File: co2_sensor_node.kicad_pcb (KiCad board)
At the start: 4 copper layers, 60 x 110 mm, 71 parts, among them J1 Conn_01x07_Female, J10 Conn_01x02_Male, J11 Conn_01x02_Male, J12 Conn_01x02_Male, J13 Conn_01x02_Male, J14 Conn_01x02, J15 Conn_01x06_Male, J2 Conn_01x04_Female, J3 Conn_01x07_Female, J4 Conn_01x04_Female, J5 Conn_01x04_Female, J6 TF-15x15, J7 SMA Female, J8 Conn_01x02_Male, J9 Conn_01x02_Male, Q1 AO3400A, Q2 AO3401A, Q3 AO3400A, Q4 AO3401A, Q5 AO3401A, SW1 K2-1102SP-C4SC-04, U1 RFM95W-868S2, U2 ublox_SAM-M8Q, U3 TPS62130, U4 TPS62130, U5 ESP32-WROOM-32D

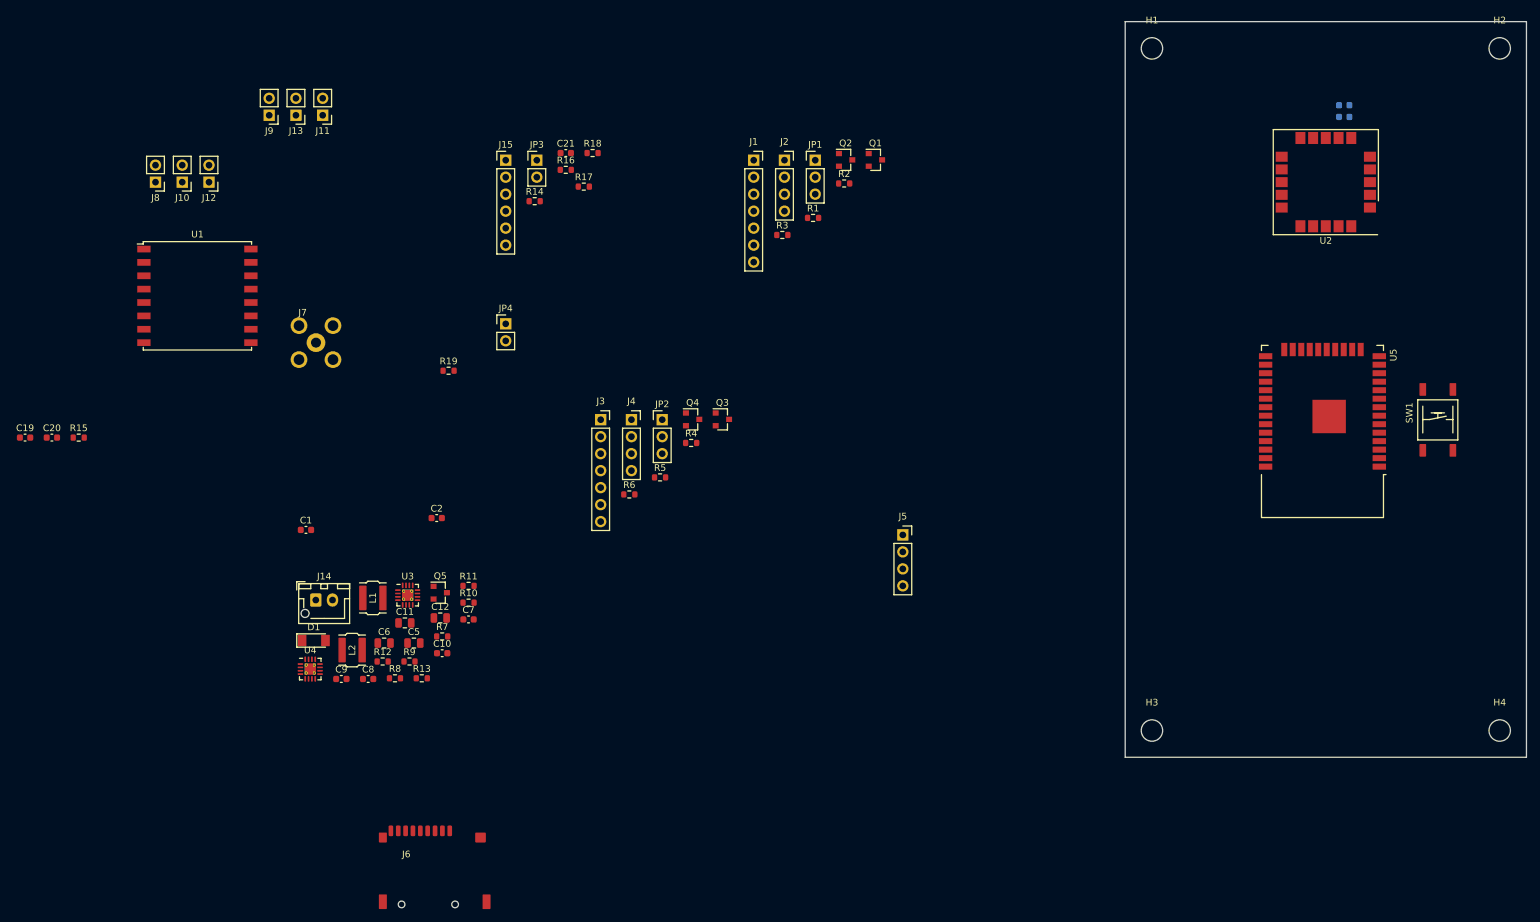
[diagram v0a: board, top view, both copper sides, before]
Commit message: First cut at layout
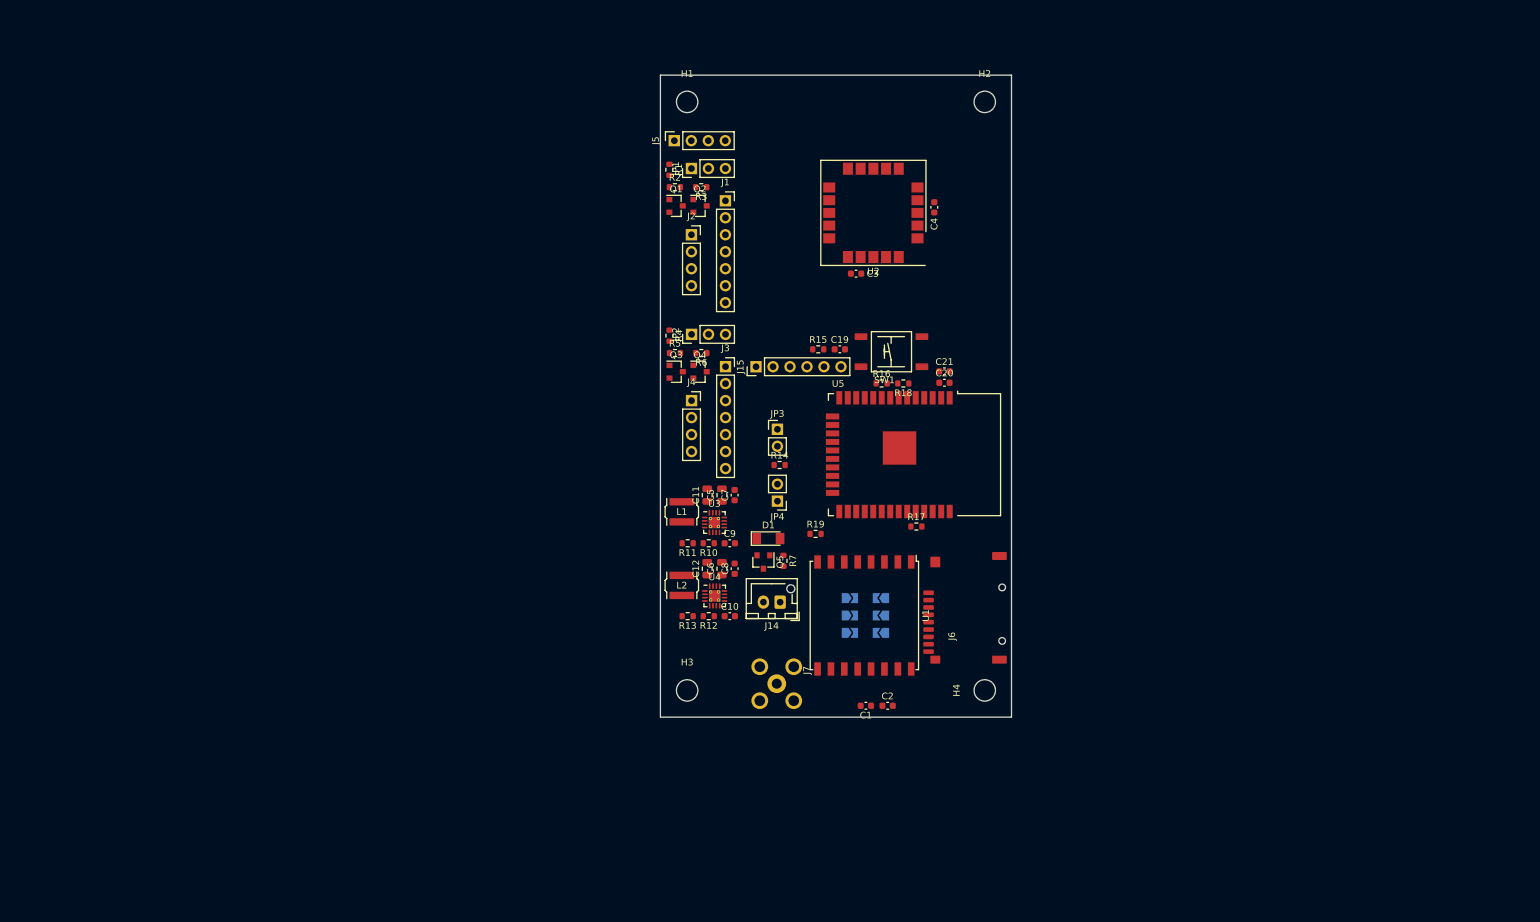
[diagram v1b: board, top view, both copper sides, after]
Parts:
- removed R8, R9: 100k, Resistor_SMD:R_0603_1608Metric
- C3, C4: moved to F.Cu
- J10, J11, J12, J13, J8, J9: footprint Connector_PinHeader_2.54mm:PinHeader_1x02_P2.54mm_Vertical -> Jumper:SolderJumper-2_P1.3mm_Open_TrianglePad1.0x1.5mm; moved to B.Cu
- moved C20 133.7 mm to (163.0, 90.0)
- moved J8 127.7 mm to (153.5, 127.4)
- moved J10 122.9 mm to (153.5, 124.8)
- moved C19 122.5 mm to (147.3, 85.0)
- moved J12 118.2 mm to (153.5, 122.2)
- moved J9 112.9 mm to (148.8, 122.2), turned to 0 degrees
- moved J13 111.6 mm to (148.8, 124.8), turned to 0 degrees
- moved R15 111.4 mm to (144.1, 85.0)
- moved U1 110.6 mm to (151.0, 124.8), turned to 270 degrees
- moved J11 110.5 mm to (148.8, 127.4), turned to 0 degrees
- moved SW1 88.9 mm to (150.5, 83.1), turned to 0 degrees
- moved C1 87.8 mm to (151.2, 138.3), turned to 180 degrees
- moved J7 85.7 mm to (137.9, 135.0), turned to 270 degrees
- moved J6 80.0 mm to (160.6, 121.4), turned to 90 degrees
- moved H2 77.4 mm to (169.0, 48.0)
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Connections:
- J11 pad 1: /LoRa Transceiver/IRQ1 -> Net-(J11-Pad1)
- J11 pad 2: Net-(J11-Pad2) -> /LoRa Transceiver/IRQ1
- J13 pad 1: /LoRa Transceiver/IRQ1 -> Net-(J13-Pad1)
- J13 pad 2: Net-(J13-Pad2) -> /LoRa Transceiver/IRQ1
- J6 pad 9: Net-(J6-Pad9) -> GND
- J9 pad 1: /LoRa Transceiver/IRQ1 -> Net-(J9-Pad1)
- J9 pad 2: Net-(J9-Pad2) -> /LoRa Transceiver/IRQ1
- JP3 pad 2: /SD Card/ENABLE -> /CO2 Sensor Connector 2/ENABLE
- R14 pad 2: /SD Card/ENABLE -> /CO2 Sensor Connector 2/ENABLE
- U1 pad 11: Net-(J13-Pad2) -> Net-(J13-Pad1)
- U1 pad 12: Net-(J11-Pad2) -> Net-(J11-Pad1)
- U1 pad 7: Net-(J9-Pad2) -> Net-(J9-Pad1)
- U5 pad 10: /CO2 Sensor Connector 1/ENABLE -> /Microprocessor section/UART2_TX
- U5 pad 11: /CO2 Sensor Connector 2/ENABLE -> /GNSS/ENABLE
- U5 pad 23: /SD Card/ENABLE -> /CO2 Sensor Connector 2/ENABLE
- U5 pad 24: /GNSS/ENABLE -> /CO2 Sensor Connector 1/ENABLE
- U5 pad 26: /Microprocessor section/I2C_SCL -> /LoRa Transceiver/CSN
- U5 pad 27: /Microprocessor section/UART2_RX -> Net-(U5-Pad27)
- U5 pad 28: /Microprocessor section/UART2_TX -> Net-(U5-Pad28)
- U5 pad 29: /Microprocessor section/I2C_SDA -> /LoRa Transceiver/IRQ2
- U5 pad 33: /LoRa Transceiver/CSN -> /LoRa Transceiver/IRQ1
- U5 pad 6: /LoRa Transceiver/IRQ1 -> /Microprocessor section/I2C_SCL
- U5 pad 7: /LoRa Transceiver/IRQ2 -> /Microprocessor section/I2C_SDA
- U5 pad 9: Net-(U5-Pad9) -> /Microprocessor section/UART2_RX
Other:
- board size 60 x 110 mm -> 52.5 x 96 mm
- rule pad_to_mask_clearance: 0 -> 0.015
- rule trace_min: 0.2 -> 0.1524
- rule via_min_drill: 0.3 -> 0.2
- rule via_min_size: 0.4 -> 0.5

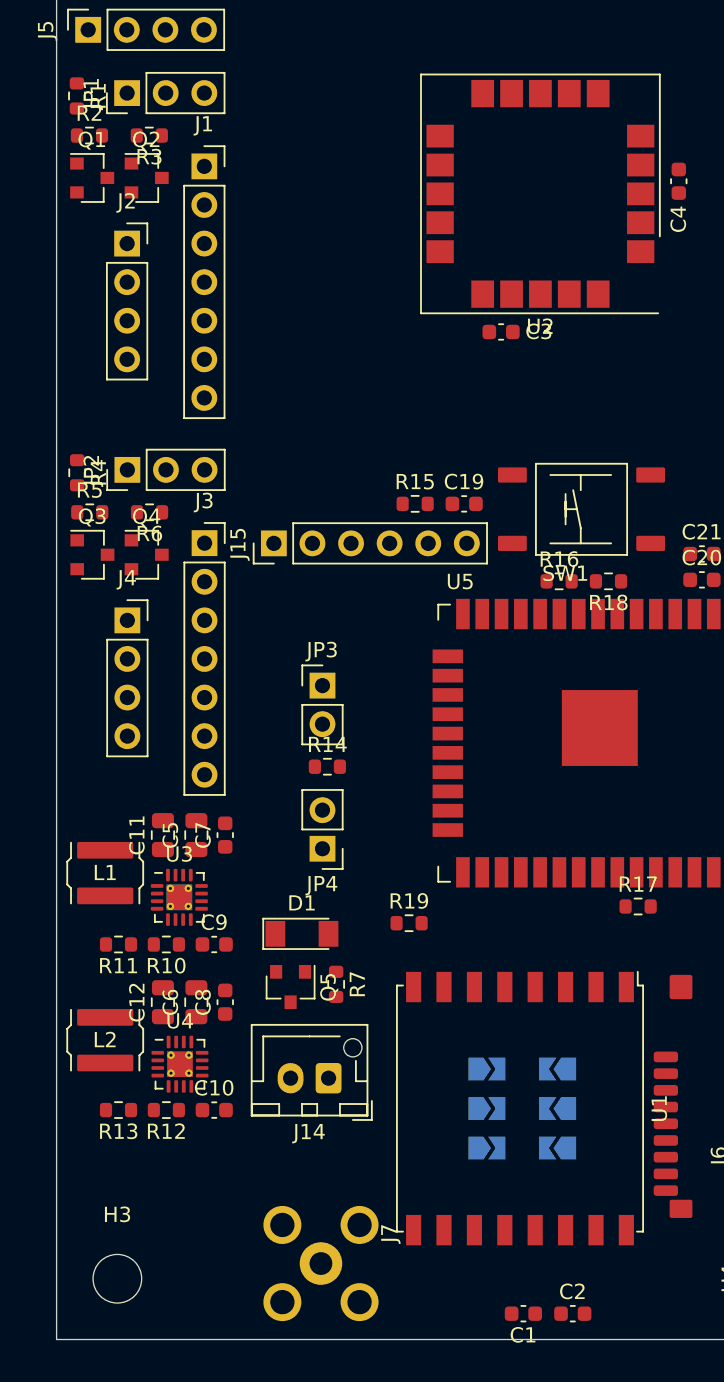
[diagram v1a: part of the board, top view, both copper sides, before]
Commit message: Start routing power section
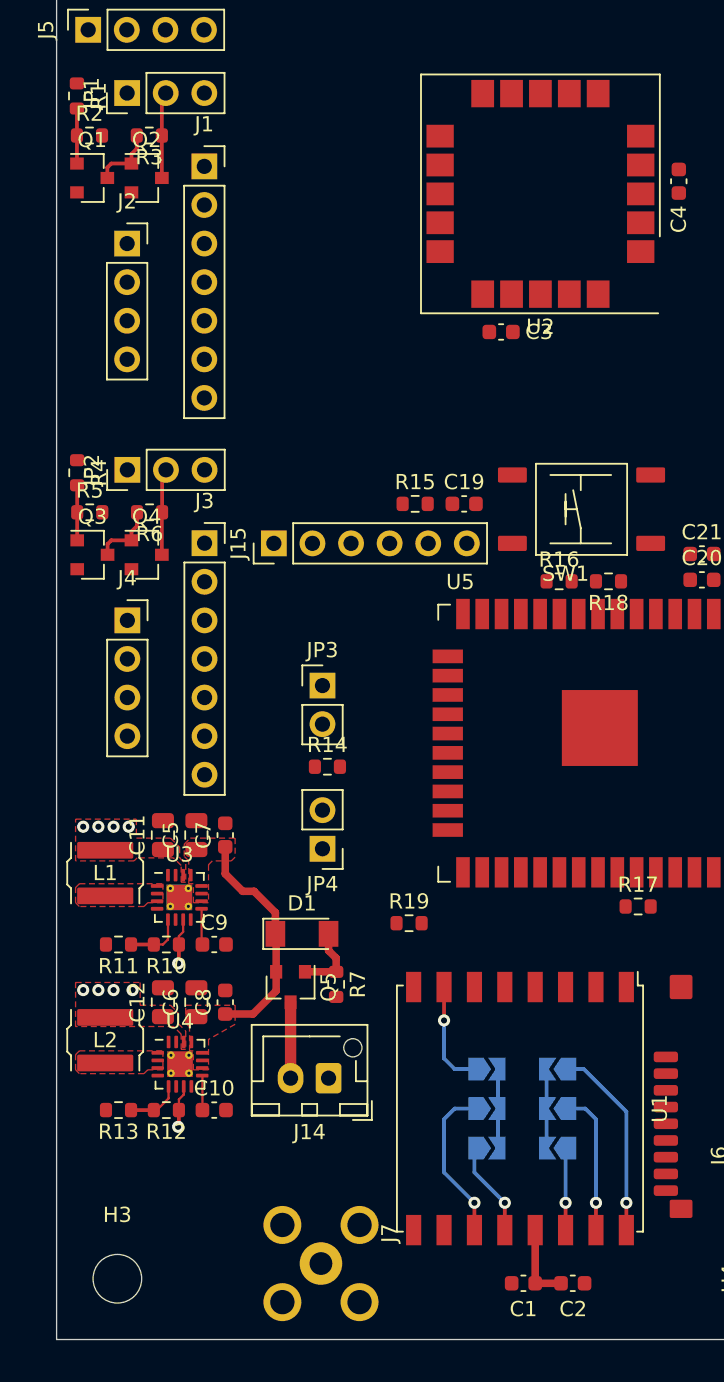
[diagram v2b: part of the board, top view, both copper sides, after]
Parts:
- moved C1 2.00 mm to (151.2, 136.3)
- moved C2 2.00 mm to (154.5, 136.3)
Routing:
- net +3V3: track 0.00 -> 18.7 mm, vias 0 -> 5
- net +BATT: track 0.00 -> 15.3 mm
- net +6V: track 0.00 -> 13.8 mm, vias 0 -> 5
- net Net-(J12-Pad1): track 0.00 -> 12.8 mm, vias 0 -> 1
- net Net-(J13-Pad1): track 0.00 -> 10.5 mm, vias 0 -> 1
- net Net-(J10-Pad1): track 0.00 -> 9.39 mm, vias 0 -> 1
- net Net-(J9-Pad1): track 0.00 -> 7.09 mm, vias 0 -> 1
- net Net-(J11-Pad1): track 0.00 -> 6.27 mm, vias 0 -> 1
- net Net-(JP2-Pad2): track 0.00 -> 5.70 mm
- net Net-(JP1-Pad2): track 0.00 -> 5.69 mm
- net Net-(J8-Pad1): track 0.00 -> 5.48 mm, vias 0 -> 1
- net /LoRa Transceiver/IRQ2: track 0.00 -> 5.20 mm
- net /LoRa Transceiver/IRQ1: track 0.00 -> 5.20 mm
- net Net-(J14-Pad2): track 0.00 -> 5.00 mm
- net Net-(D1-Pad2): track 0.00 -> 4.76 mm
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- added copper zone on F.Cu, net +3V3
- added copper zone on F.Cu, net +6V
- added copper zone on F.Cu, net +BATT
- added copper zone on In1.Cu, net GND
- added copper zone on F.Cu, net Net-(L1-Pad1)
- added copper zone on F.Cu, net Net-(L2-Pad1)

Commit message: Layout complete, barring review and polish
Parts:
- added BOARD_FIDUCIAL: Fiducial_1mm_Mask2mm, Fiducial:Fiducial_1mm_Mask2mm, F.Cu at (129.5, 136.0)
- added BOARD_FIDUCIAL: Fiducial_1mm_Mask2mm, Fiducial:Fiducial_1mm_Mask2mm, F.Cu at (129.5, 48.0)
- added BOARD_FIDUCIAL: Fiducial_1mm_Mask2mm, Fiducial:Fiducial_1mm_Mask2mm, F.Cu at (163.5, 136.0)
- added REF**: JLCPCB_TOOLING_HOLE, co2_sensor_node_rel:JLCPCB_TOOLING_HOLE, F.Cu at (171.5, 45.5)
- added REF**: JLCPCB_TOOLING_HOLE, co2_sensor_node_rel:JLCPCB_TOOLING_HOLE, F.Cu at (122.0, 138.5)
- added REF**: JLCPCB_TOOLING_HOLE, co2_sensor_node_rel:JLCPCB_TOOLING_HOLE, F.Cu at (122.0, 45.5)
- added REF**: JLCPCB_TOOLING_HOLE, co2_sensor_node_rel:JLCPCB_TOOLING_HOLE, F.Cu at (171.5, 138.5)
- added REF**: ESD-Logo_8.9x8mm_SilkScreen, Symbol:ESD-Logo_8.9x8mm_SilkScreen, F.Cu at (165.5, 76.0)
- moved JP3 8.29 mm to (140.7, 104.8), turned to 270 degrees
- moved R14 5.63 mm to (143.7, 104.0), turned to 270 degrees
- moved R19 5.53 mm to (149.2, 113.2)
- moved JP4 2.88 mm to (140.7, 108.7), turned to 270 degrees
- moved R16 1.51 mm to (155.1, 89.9)
- moved R18 1.51 mm to (158.3, 89.9)
- moved R17 0.76 mm to (159.5, 111.6)
- moved C10 0.51 mm to (131.4, 125.0)
- moved R12 0.51 mm to (128.2, 125.0)
- moved R13 0.51 mm to (125.1, 125.0)
- moved C11 0.50 mm to (128.0, 106.8)
- moved C12 0.50 mm to (128.0, 117.8)
- moved C5 0.50 mm to (130.2, 106.8)
- moved C6 0.50 mm to (130.2, 117.8)
- moved C7 0.50 mm to (132.1, 106.8)
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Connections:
- JP3 pad 1: +3V3 -> /CO2 Sensor Connector 2/ENABLE
- JP3 pad 2: /CO2 Sensor Connector 2/ENABLE -> +3V3
- R16 pad 2: /Microprocessor section/I2C_SDA -> /Microprocessor section/I2C_SCL
- R18 pad 2: /Microprocessor section/I2C_SCL -> /Microprocessor section/I2C_SDA
- U5 pad 10: /Microprocessor section/UART2_TX -> /Microprocessor section/UART2_RX
- U5 pad 29: /LoRa Transceiver/IRQ2 -> /LoRa Transceiver/IRQ1
- U5 pad 33: /LoRa Transceiver/IRQ1 -> /LoRa Transceiver/IRQ2
- U5 pad 6: /Microprocessor section/I2C_SCL -> /Microprocessor section/I2C_SDA
- U5 pad 7: /Microprocessor section/I2C_SDA -> /Microprocessor section/I2C_SCL
- U5 pad 9: /Microprocessor section/UART2_RX -> /Microprocessor section/UART2_TX
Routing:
- net GND: track 0.00 -> 144.2 mm, vias 0 -> 201
- net /Microprocessor section/I2C_SDA: track 0.00 -> 80.3 mm, vias 0 -> 2
- net /CO2 Sensor Connector 1/ENABLE: track 0.00 -> 70.1 mm, vias 0 -> 2
- net /Microprocessor section/I2C_SCL: track 0.00 -> 62.5 mm, vias 0 -> 2
- net +6V: track 13.8 -> 72.5 mm, vias 5 -> 6
- net /Microprocessor section/UART1_RX: track 0.00 -> 47.2 mm, vias 0 -> 1
- net /CO2 Sensor Connector 2/ENABLE: track 0.00 -> 43.8 mm, vias 0 -> 1
- net /Microprocessor section/UART1_TX: track 0.00 -> 43.0 mm, vias 0 -> 1
- net +3V3: track 18.7 -> 60.7 mm, vias 5 -> 20
- net /Microprocessor section/BOOT: track 0.00 -> 41.1 mm, vias 0 -> 1
- net /CO2 Sensor Connector 1/N_RDY: track 0.00 -> 35.6 mm
- net /Microprocessor section/RXD0: track 0.00 -> 34.8 mm, vias 0 -> 1
- net /Microprocessor section/TXD0: track 0.00 -> 34.2 mm, vias 0 -> 1
- net /Microprocessor section/UART2_TX: track 0.00 -> 32.5 mm, vias 0 -> 1
- net /Microprocessor section/UART2_RX: track 0.00 -> 31.3 mm, vias 0 -> 1
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- added copper zone on In2.Cu, net +3V3
- added copper zone on B.Cu, net GND
- added copper zone on F.Cu, net GND
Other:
- outline, holes or cut-outs redrawn
- board text added: "+ - VIN 6-9V"
- board text added: "+3V3 GND RXD0 TXD0 EN BOOT"
- board text added: "0-NORM 1-PROG"
- board text added: "0-OFF 1-ON U0 DEBUG"
- board text added: "0x42"
- board text added: "0x76/0x77"
- board text added: "1"
- board text added: "6V VCC 3V"
- board text added: "<0V"
- board text added: "<3V"
- board text added: "<6V"
- board text added: "BME280"
- board text added: "BOARD STACKUP: JLC7628"
- board text added: "BOOT MODE"
- board text added: "DIO2 DIO1 DIO0"
- board text added: "DIO5 DIO3 DIO4"
- board text added: "GND"
- board text added: "IRQ1"
- board text added: "IRQ2"
- board text added: "LoRa ANT"
- board text added: "NC"
- board text added: "RDY"
- board text added: "RESET"
- board text added: "RX"
- board text added: "SDA SCL GND 3V3"
- board text added: "SENSOR 1"
- board text added: "SENSOR 2"
- board text added: "TX"
- board text added: "VCC"
- board text added: "Voltage select Sensor 1"

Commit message: Export fabrication files
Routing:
- net GND: vias 201 -> 207
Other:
- board text added: "+ - VIN 6-15V"
- board text removed: "+ - VIN 6-9V"
